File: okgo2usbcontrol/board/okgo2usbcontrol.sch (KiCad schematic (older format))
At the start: 22 parts

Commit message: switches for okgo2 mini and usb
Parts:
- SW?: Farnell (none) -> 2610947
- SW?: Farnell (none) -> 2435152
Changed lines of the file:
@@
 F 1 "FIRE" H 2700 4214 50  0000 C CNN
 F 2 "" H 2700 4050 50  0001 C CNN
-F 3 "" H 2700 4050 50  0001 C CNN
+F 3 "http://www.farnell.com/datasheets/2074946.pdf" H 2700 4050 50  0001 C CNN
+F 4 "2610947" H 2700 4050 60  0001 C CNN "Farnell"
 	1    2700 4050
 	1    0    0    -1
@@
 F 1 "ARM" H 5350 5664 50  0000 C CNN
 F 2 "" H 5350 5500 50  0001 C CNN
-F 3 "" H 5350 5500 50  0001 C CNN
+F 3 "http://www.farnell.com/datasheets/1839855.pdf" H 5350 5500 50  0001 C CNN
+F 4 "2435152" H 5350 5500 60  0001 C CNN "Farnell"
 	1    5350 5500
 	1    0    0    -1

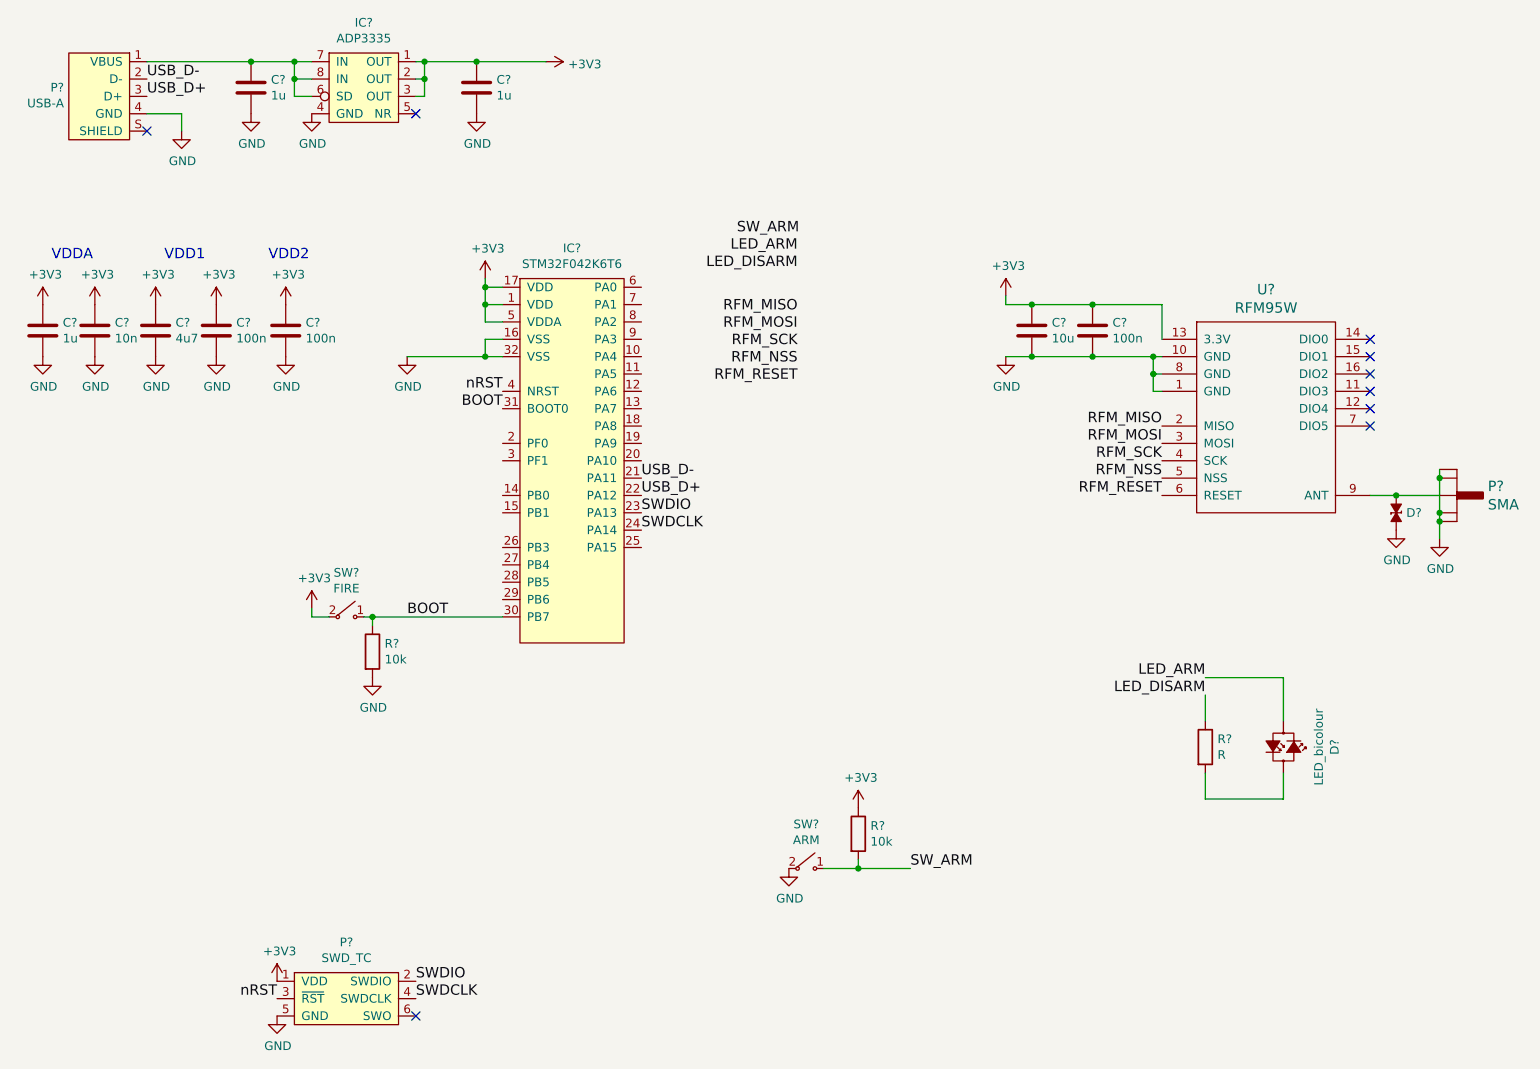
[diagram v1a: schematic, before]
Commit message: footprints for okgo2mini and usbcontrol
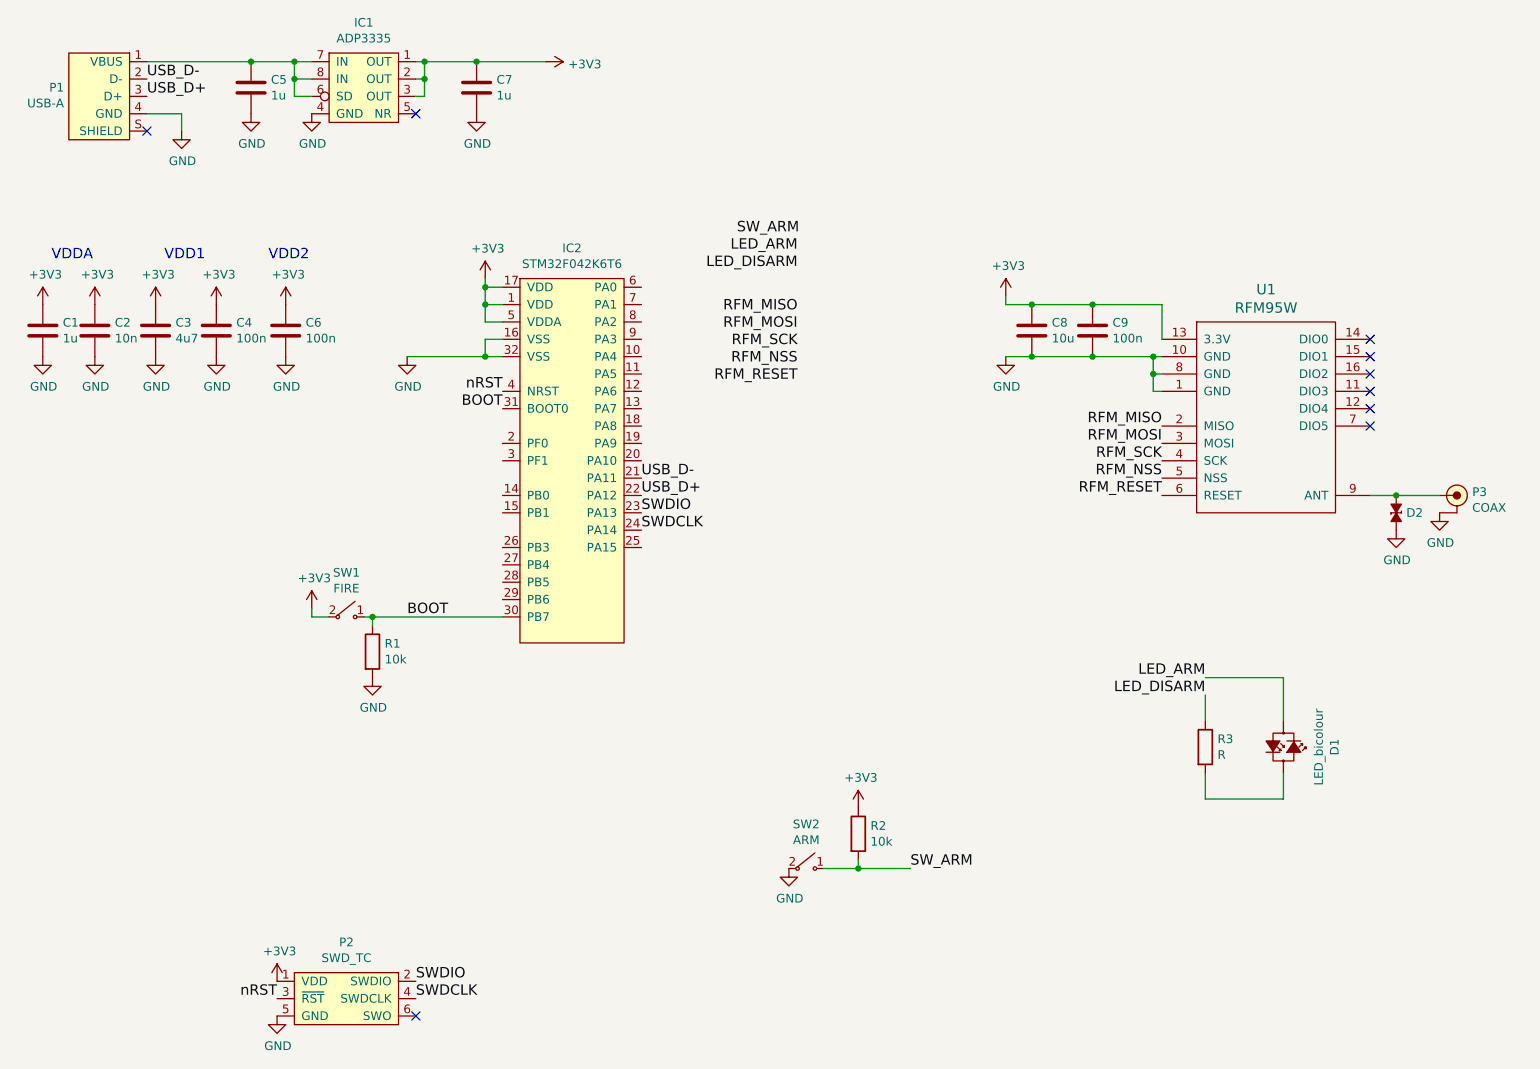
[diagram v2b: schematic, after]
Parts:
- removed P?: SMA, agg:SMA-EDGE, symbol SMA
- added P3: COAX, agg:SMA-EDGE, symbol COAX
- C1, C2, C3, C4, C5, C6, C7, C8, C9: renamed from C?; footprint (none) -> agg:0603
- D1: renamed from D?; footprint (none) -> agg:0805-LED
- D2: renamed from D?; footprint agg:0402 -> agg:0603; Farnell 2368169 -> (none)
- P1: renamed from P?; footprint (none) -> footprints:USB-A_M_Edge
- R1, R2, R3: renamed from R?; footprint (none) -> agg:0603
- SW1: renamed from SW?; footprint (none) -> footprints:FSM2JSMx
- SW2: renamed from SW?; footprint (none) -> footprints:JSX08001SAQNL
- U1: renamed from U?; footprint (none) -> footprints:RFM95W
- gave numbers to parts that had none: 3
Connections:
- net GND: now also P3.2 (GND)
- net at D2.1, U1.9 (ANT): now also P3.1 (RF)

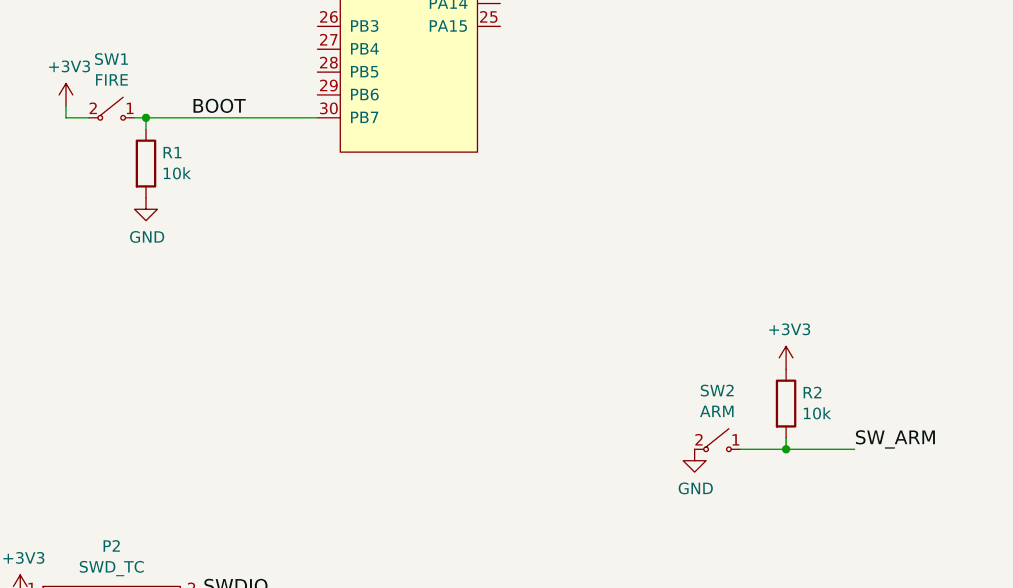
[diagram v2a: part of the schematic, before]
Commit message: Minified parts, did some order codes
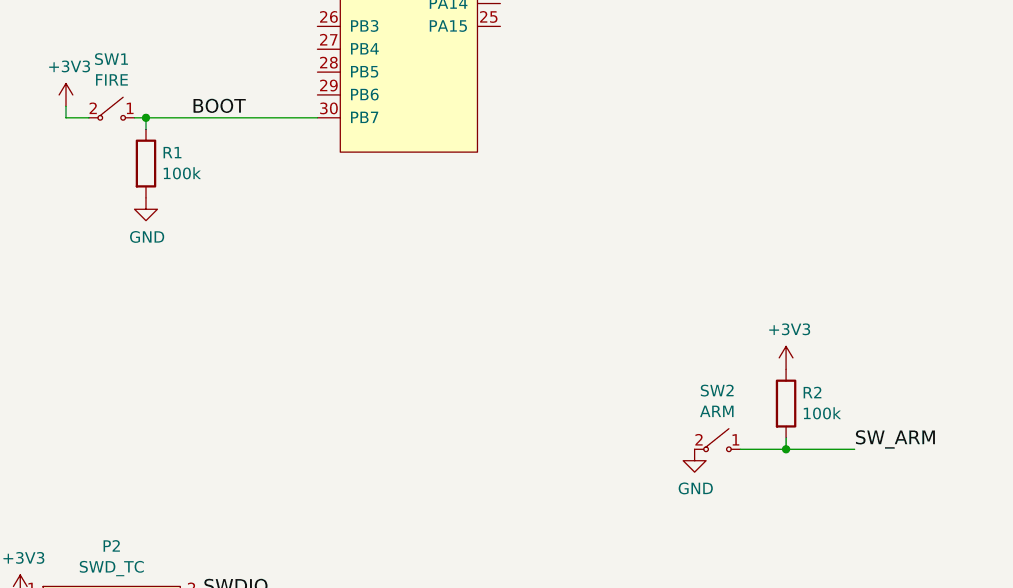
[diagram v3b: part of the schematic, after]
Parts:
- R1, R2: value 10k -> 100k
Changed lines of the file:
@@
 $EndComp
 $Comp
-L +3V3 #PWR16
+L +3V3 #PWR01
 U 1 1 59971DC0
 P 2500 4000
-F 0 "#PWR16" H 2500 3850 50  0001 C CNN
+F 0 "#PWR01" H 2500 3850 50  0001 C CNN
 F 1 "+3V3" H 2515 4173 50  0000 C CNN
 F 2 "" H 2500 4000 50  0001 C CNN
@@
 P 2850 4250
 F 0 "R1" H 2920 4296 50  0000 L CNN
-F 1 "10k" H 2920 4205 50  0000 L CNN
+F 1 "100k" H 2920 4205 50  0000 L CNN
 F 2 "agg:0603" V 2780 4250 50  0001 C CNN
 F 3 "" H 2850 4250 50  0001 C CNN
@@
 BOOT
 $Comp
-L GND #PWR17
+L GND #PWR02
 U 1 1 59972159
 P 2850 4400
-F 0 "#PWR17" H 2850 4150 50  0001 C CNN
+F 0 "#PWR02" H 2850 4150 50  0001 C CNN
 F 1 "GND" H 2855 4227 50  0000 C CNN
 F 2 "" H 2850 4400 50  0001 C CNN
@@
 USB_D+
 $Comp
-L GND #PWR7
+L GND #PWR03
 U 1 1 59972A6E
 P 1750 1250
-F 0 "#PWR7" H 1750 1000 50  0001 C CNN
+F 0 "#PWR03" H 1750 1000 50  0001 C CNN
 F 1 "GND" H 1755 1077 50  0000 C CNN
 F 2 "" H 1750 1250 50  0001 C CNN
@@
 Connection ~ 2400 950
 $Comp
-L GND #PWR15
+L GND #PWR04
 U 1 1 59972E27
 P 2500 1150
-F 0 "#PWR15" H 2500 900 50  0001 C CNN
+F 0 "#PWR04" H 2500 900 50  0001 C CNN
 F 1 "GND" H 2505 977 50  0000 C CNN
 F 2 "" H 2500 1150 50  0001 C CNN
@@
 $EndComp
 $Comp
-L GND #PWR10
+L GND #PWR05
 U 1 1 59972F12
 P 2150 1150
-F 0 "#PWR10" H 2150 900 50  0001 C CNN
+F 0 "#PWR05" H 2150 900 50  0001 C CNN
 F 1 "GND" H 2155 977 50  0000 C CNN
 F 2 "" H 2150 1150 50  0001 C CNN
@@
 NoConn ~ 3100 1150
 $Comp
-L GND #PWR19
+L GND #PWR06
 U 1 1 5997316D
 P 3450 1150
-F 0 "#PWR19" H 3450 900 50  0001 C CNN
+F 0 "#PWR06" H 3450 900 50  0001 C CNN
 F 1 "GND" H 3455 977 50  0000 C CNN
 F 2 "" H 3450 1150 50  0001 C CNN
@@
 Connection ~ 3450 850
 $Comp
-L +3V3 #PWR21
+L +3V3 #PWR07
 U 1 1 599731F0
 P 3850 850
-F 0 "#PWR21" H 3850 700 50  0001 C CNN
+F 0 "#PWR07" H 3850 700 50  0001 C CNN
 F 1 "+3V3" V 3865 978 50  0000 L CNN
 F 2 "" H 3850 850 50  0001 C CNN
@@
 $EndComp
 $Comp
-L +3V3 #PWR11
+L +3V3 #PWR08
 U 1 1 59973895
 P 2300 6150
-F 0 "#PWR11" H 2300 6000 50  0001 C CNN
+F 0 "#PWR08" H 2300 6000 50  0001 C CNN
 F 1 "+3V3" H 2315 6323 50  0000 C CNN
 F 2 "" H 2300 6150 50  0001 C CNN
@@
 $EndComp
 $Comp
-L GND #PWR12
+L GND #PWR09
 U 1 1 59973BD8
 P 2300 6350
-F 0 "#PWR12" H 2300 6100 50  0001 C CNN
+F 0 "#PWR09" H 2300 6100 50  0001 C CNN
 F 1 "GND" H 2305 6177 50  0000 C CNN
 F 2 "" H 2300 6350 50  0001 C CNN
@@
 Connection ~ 8750 3350
 $Comp
-L GND #PWR26
+L GND #PWR010
 U 1 1 5997559E
 P 8750 3550
-F 0 "#PWR26" H 8750 3300 50  0001 C CNN
+F 0 "#PWR010" H 8750 3300 50  0001 C CNN
 F 1 "GND" H 8755 3377 50  0000 C CNN
 F 2 "" H 8750 3550 50  0001 C CNN
@@
 $EndComp
 $Comp
-L GND #PWR27
+L GND #PWR011
 U 1 1 599755E7
 P 9000 3450
-F 0 "#PWR27" H 9000 3200 50  0001 C CNN
+F 0 "#PWR011" H 9000 3200 50  0001 C CNN
 F 1 "GND" H 9005 3277 50  0000 C CNN
 F 2 "" H 9000 3450 50  0001 C CNN
@@
 NoConn ~ 8600 2950
 $Comp
-L +3V3 #PWR24
+L +3V3 #PWR012
 U 1 1 59975A59
 P 6500 2200
-F 0 "#PWR24" H 6500 2050 50  0001 C CNN
+F 0 "#PWR012" H 6500 2050 50  0001 C CNN
 F 1 "+3V3" H 6515 2373 50  0000 C CNN
 F 2 "" H 6500 2200 50  0001 C CNN
@@
 Connection ~ 7000 2550
 $Comp
-L GND #PWR25
+L GND #PWR013
 U 1 1 59975EC5
 P 6500 2550
-F 0 "#PWR25" H 6500 2300 50  0001 C CNN
+F 0 "#PWR013" H 6500 2300 50  0001 C CNN
 F 1 "GND" H 6505 2377 50  0000 C CNN
 F 2 "" H 6500 2550 50  0001 C CNN
@@
 RFM_RESET
 $Comp
-L GND #PWR22
+L GND #PWR014
 U 1 1 5997659A
 P 5250 5500
-F 0 "#PWR22" H 5250 5250 50  0001 C CNN
+F 0 "#PWR014" H 5250 5250 50  0001 C CNN
 F 1 "GND" H 5255 5327 50  0000 C CNN
 F 2 "" H 5250 5500 50  0001 C CNN
@@
 P 5650 5300
 F 0 "R2" H 5720 5346 50  0000 L CNN
-F 1 "10k" H 5720 5255 50  0000 L CNN
+F 1 "100k" H 5720 5255 50  0000 L CNN
 F 2 "agg:0603" V 5580 5300 50  0001 C CNN
 F 3 "" H 5650 5300 50  0001 C CNN
@@
 $EndComp
 $Comp
-L +3V3 #PWR23
+L +3V3 #PWR015
 U 1 1 5997679F
 P 5650 5150
-F 0 "#PWR23" H 5650 5000 50  0001 C CNN
+F 0 "#PWR015" H 5650 5000 50  0001 C CNN
 F 1 "+3V3" H 5665 5323 50  0000 C CNN
 F 2 "" H 5650 5150 50  0001 C CNN
@@
 LED_DISARM
 $Comp
-L +3V3 #PWR20
+L +3V3 #PWR016
 U 1 1 59977C42
 P 3500 2100
-F 0 "#PWR20" H 3500 1950 50  0001 C CNN
+F 0 "#PWR016" H 3500 1950 50  0001 C CNN
 F 1 "+3V3" H 3515 2273 50  0000 C CNN
 F 2 "" H 3500 2100 50  0001 C CNN
@@
 Connection ~ 3500 2250
 $Comp
-L GND #PWR18
+L GND #PWR017
 U 1 1 59978002
 P 3050 2550
-F 0 "#PWR18" H 3050 2300 50  0001 C CNN
+F 0 "#PWR017" H 3050 2300 50  0001 C CNN
 F 1 "GND" H 3055 2377 50  0000 C CNN
 F 2 "" H 3050 2550 50  0001 C CNN
@@
 $EndComp
 $Comp
-L +3V3 #PWR1
+L +3V3 #PWR018
 U 1 1 5997941A
 P 950 2250
-F 0 "#PWR1" H 950 2100 50  0001 C CNN
+F 0 "#PWR018" H 950 2100 50  0001 C CNN
 F 1 "+3V3" H 965 2423 50  0000 C CNN
 F 2 "" H 950 2250 50  0001 C CNN
@@
 $EndComp
 $Comp
-L +3V3 #PWR3
+L +3V3 #PWR019
 U 1 1 59979458
 P 1250 2250
-F 0 "#PWR3" H 1250 2100 50  0001 C CNN
+F 0 "#PWR019" H 1250 2100 50  0001 C CNN
 F 1 "+3V3" H 1265 2423 50  0000 C CNN
 F 2 "" H 1250 2250 50  0001 C CNN
@@
 $EndComp
 $Comp
-L +3V3 #PWR5
+L +3V3 #PWR020
 U 1 1 5997948F
 P 1600 2250
-F 0 "#PWR5" H 1600 2100 50  0001 C CNN
+F 0 "#PWR020" H 1600 2100 50  0001 C CNN
 F 1 "+3V3" H 1615 2423 50  0000 C CNN
 F 2 "" H 1600 2250 50  0001 C CNN
@@
 $EndComp
 $Comp
-L +3V3 #PWR8
+L +3V3 #PWR021
 U 1 1 59979512
 P 1950 2250
-F 0 "#PWR8" H 1950 2100 50  0001 C CNN
+F 0 "#PWR021" H 1950 2100 50  0001 C CNN
 F 1 "+3V3" H 1965 2423 50  0000 C CNN
 F 2 "" H 1950 2250 50  0001 C CNN
@@
 $EndComp
 $Comp
-L +3V3 #PWR13
+L +3V3 #PWR022
 U 1 1 59979549
 P 2350 2250
-F 0 "#PWR13" H 2350 2100 50  0001 C CNN
+F 0 "#PWR022" H 2350 2100 50  0001 C CNN
 F 1 "+3V3" H 2365 2423 50  0000 C CNN
 F 2 "" H 2350 2250 50  0001 C CNN
@@
 $EndComp
 $Comp
-L GND #PWR2
+L GND #PWR023
 U 1 1 599795BB
 P 950 2550
-F 0 "#PWR2" H 950 2300 50  0001 C CNN
+F 0 "#PWR023" H 950 2300 50  0001 C CNN
 F 1 "GND" H 955 2377 50  0000 C CNN
 F 2 "" H 950 2550 50  0001 C CNN
@@
 $EndComp
 $Comp
-L GND #PWR4
+L GND #PWR024
 U 1 1 599795F9
 P 1250 2550
-F 0 "#PWR4" H 1250 2300 50  0001 C CNN
+F 0 "#PWR024" H 1250 2300 50  0001 C CNN
 F 1 "GND" H 1255 2377 50  0000 C CNN
 F 2 "" H 1250 2550 50  0001 C CNN
@@
 $EndComp
 $Comp
-L GND #PWR6
+L GND #PWR025
 U 1 1 59979630
 P 1600 2550
-F 0 "#PWR6" H 1600 2300 50  0001 C CNN
+F 0 "#PWR025" H 1600 2300 50  0001 C CNN
 F 1 "GND" H 1605 2377 50  0000 C CNN
 F 2 "" H 1600 2550 50  0001 C CNN
@@
 $EndComp
 $Comp
-L GND #PWR9
+L GND #PWR026
 U 1 1 59979667
 P 1950 2550
-F 0 "#PWR9" H 1950 2300 50  0001 C CNN
+F 0 "#PWR026" H 1950 2300 50  0001 C CNN
 F 1 "GND" H 1955 2377 50  0000 C CNN
 F 2 "" H 1950 2550 50  0001 C CNN
@@
 $EndComp
 $Comp
-L GND #PWR14
+L GND #PWR027
 U 1 1 5997969E
 P 2350 2550
-F 0 "#PWR14" H 2350 2300 50  0001 C CNN
+F 0 "#PWR027" H 2350 2300 50  0001 C CNN
 F 1 "GND" H 2355 2377 50  0000 C CNN
 F 2 "" H 2350 2550 50  0001 C CNN
